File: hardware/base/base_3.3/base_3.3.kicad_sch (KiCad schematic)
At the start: 8 parts, among them IC1 single_pad_smd, IC2 single_pad_smd, J1 Conn 1, J2 Conn 2

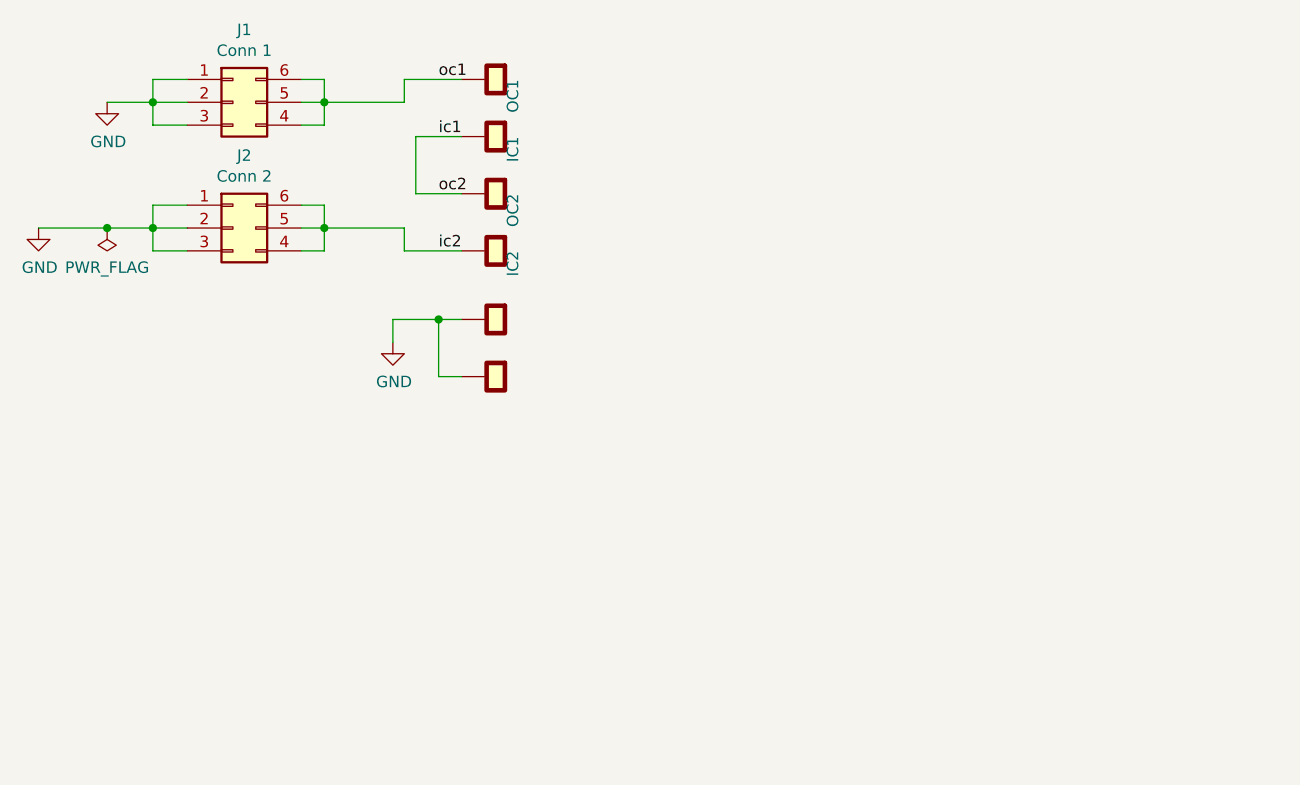
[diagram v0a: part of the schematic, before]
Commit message: Base 3.3 updated to v2
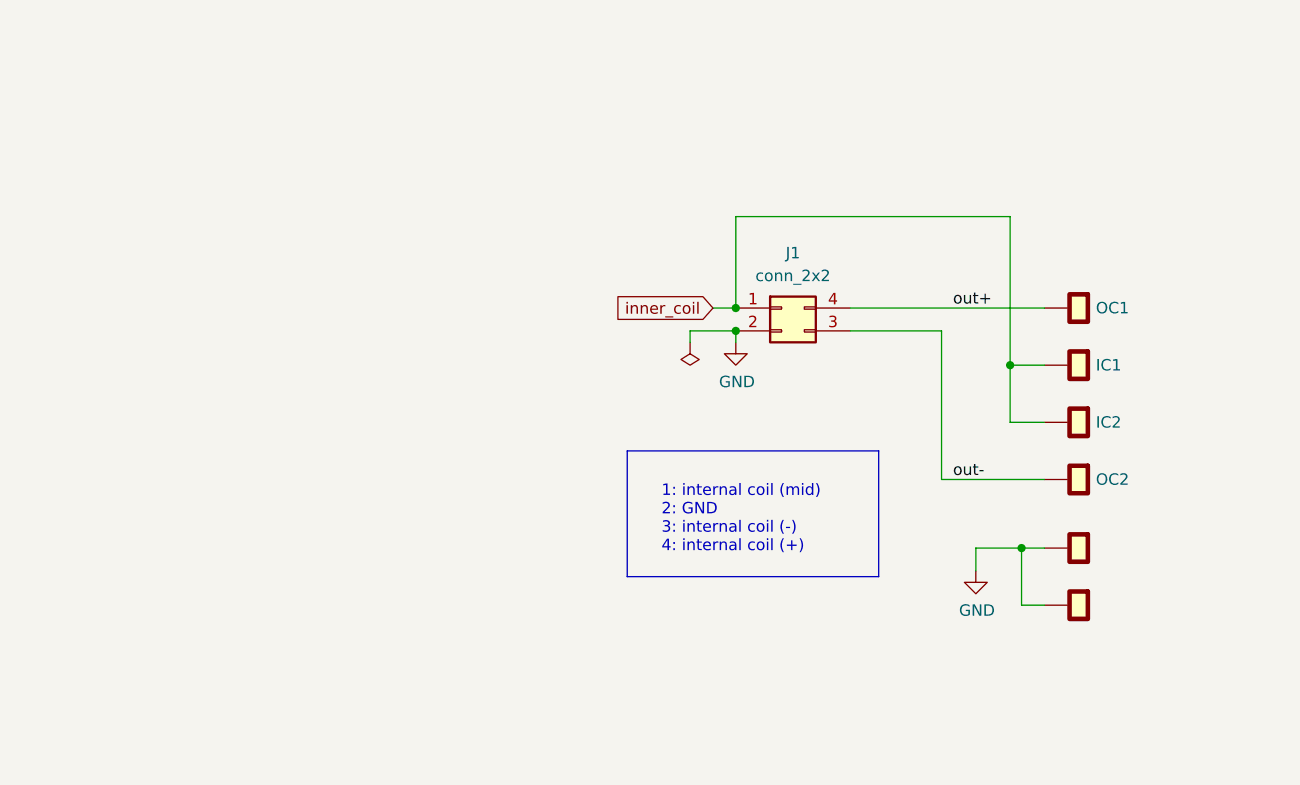
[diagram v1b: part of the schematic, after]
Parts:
- removed J1: Conn 1, cycfi_library:pin_header_2x3p_1.00mm_smd_vertical, symbol Connector_Generic:Conn_02x03_Counter_Clockwise
- removed J2: Conn 2, cycfi_library:pin_header_2x3p_1.00mm_smd_vertical, symbol Connector_Generic:Conn_02x03_Counter_Clockwise
- added J1: conn_2x2, cycfi_library:pin_header_2x2p_2.00mm_smd_vertical, symbol Connector_Generic:Conn_02x02_Counter_Clockwise
- H5, H6: value single_pad_smd -> single_pad; footprint cycfi_library:single-pad-3x2 -> xr_spectra_library:rail_slot_3.3; symbol cycfi_library:single_pad_smd -> cycfi_library:single_pad
- IC1, IC2, OC1, OC2: value single_pad_smd -> single_pad; footprint cycfi_library:single-pad-2x2-th -> cycfi_library:single-pad-1.6x1.6_circular; symbol cycfi_library:single_pad_smd -> cycfi_library:single_pad
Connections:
- net ic2 is gone; now on net inner_coil: IC2.1
- net GND: now also J1.2 (Pin_2)
- net ic1 renamed inner_coil
- net inner_coil: now also J1.1 (Pin_1); no longer OC2.1
- net oc1 renamed out+
- net out+: now also J1.4 (Pin_4)
- new net out-: J1.3 (Pin_3), OC2.1
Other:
- note added: "1: internal coil (mid) 2: GND 3: internal coil (-) 4: internal coil (+)"
- moved on the sheet: IC1, IC2, OC1, OC2

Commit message: fixed schematics
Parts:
- renumbered OC1 to IC1, OC2 to IC2, IC1 to OC1, IC2 to OC2
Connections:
- net inner_coil renamed middle_coil
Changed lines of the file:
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@@
     (stroke (width 0) (type default) (color 0 0 0 0))
   )
-  (polyline (pts (xy 123.825 86.995) (xy 123.825 100.965))
+  (polyline (pts (xy 123.19 87.63) (xy 123.19 101.6))
     (stroke (width 0) (type default) (color 0 0 0 0))
   )
@@
     (stroke (width 0) (type default) (color 0 0 0 0))
   )
-  (polyline (pts (xy 123.825 86.995) (xy 151.765 86.995))
+  (polyline (pts (xy 123.19 87.63) (xy 152.4 87.63))
     (stroke (width 0) (type default) (color 0 0 0 0))
   )
@@
     (stroke (width 0) (type default) (color 0 0 0 0))
   )
-  (polyline (pts (xy 151.765 100.965) (xy 123.825 100.965))
+  (polyline (pts (xy 152.4 101.6) (xy 123.19 101.6))
     (stroke (width 0) (type default) (color 0 0 0 0))
   )
@@
     (stroke (width 0) (type default) (color 0 0 0 0))
   )
-  (polyline (pts (xy 151.765 86.995) (xy 151.765 100.965))
+  (polyline (pts (xy 152.4 87.63) (xy 152.4 101.6))
     (stroke (width 0) (type default) (color 0 0 0 0))
   )
@@
     (effects (font (size 1.27 1.27)) (justify left bottom))
   )
-  (global_label "inner_coil" (shape input) (at 133.35 71.12 180) (fields_autoplaced)
+  (global_label "middle_coil" (shape input) (at 133.35 71.12 180) (fields_autoplaced)
     (effects (font (size 1.27 1.27)) (justify right))
-    (property "Intersheet References" "${INTERSHEET_REFS}" (id 0) (at 121.7729 71.0406 0)
+    (property "Intersheet References" "${INTERSHEET_REFS}" (id 0) (at 120.2006 71.0406 0)
       (effects (font (size 1.27 1.27)) (justify right) hide)
     )
@@
   (symbol (lib_id "cycfi_library:single_pad") (at 172.72 71.12 270) (unit 1)
     (in_bom yes) (on_board yes)
-    (property "Reference" "OC1" (id 0) (at 175.895 71.12 90)
+    (property "Reference" "IC1" (id 0) (at 175.895 71.12 90)
       (effects (font (size 1.27 1.27)) (justify left))
     )
@@
   (symbol (lib_id "cycfi_library:single_pad") (at 172.72 77.47 270) (unit 1)
     (in_bom yes) (on_board yes)
-    (property "Reference" "IC1" (id 0) (at 175.895 77.47 90)
+    (property "Reference" "OC1" (id 0) (at 175.895 77.47 90)
       (effects (font (size 1.27 1.27)) (justify left))
     )
@@
   (symbol (lib_id "cycfi_library:single_pad") (at 172.72 90.17 270) (unit 1)
     (in_bom yes) (on_board yes)
-    (property "Reference" "OC2" (id 0) (at 175.895 90.17 90)
+    (property "Reference" "IC2" (id 0) (at 175.895 90.17 90)
       (effects (font (size 1.27 1.27)) (justify left))
     )
@@
   (symbol (lib_id "cycfi_library:single_pad") (at 172.72 83.82 270) (unit 1)
     (in_bom yes) (on_board yes)
-    (property "Reference" "IC2" (id 0) (at 175.895 83.82 90)
+    (property "Reference" "OC2" (id 0) (at 175.895 83.82 90)
       (effects (font (size 1.27 1.27)) (justify left))
     )
@@
       (reference "H6") (unit 1) (value "single_pad") (footprint "xr_spectra_library:rail_slot_3.3")
     )
-    (path "/00000000-0000-0000-0000-000061122fed"
+    (path "/00000000-0000-0000-0000-000061122909"
       (reference "IC1") (unit 1) (value "single_pad") (footprint "cycfi_library:single-pad-1.6x1.6_circular")
     )
-    (path "/00000000-0000-0000-0000-0000611302a2"
+    (path "/00000000-0000-0000-0000-00006112ffae"
       (reference "IC2") (unit 1) (value "single_pad") (footprint "cycfi_library:single-pad-1.6x1.6_circular")
     )
@@
       (reference "J1") (unit 1) (value "conn_2x2") (footprint "cycfi_library:pin_header_2x2p_2.00mm_smd_vertical")
     )
-    (path "/00000000-0000-0000-0000-000061122909"
+    (path "/00000000-0000-0000-0000-000061122fed"
       (reference "OC1") (unit 1) (value "single_pad") (footprint "cycfi_library:single-pad-1.6x1.6_circular")
     )
-    (path "/00000000-0000-0000-0000-00006112ffae"
+    (path "/00000000-0000-0000-0000-0000611302a2"
       (reference "OC2") (unit 1) (value "single_pad") (footprint "cycfi_library:single-pad-1.6x1.6_circular")
     )

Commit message: Base 3.3 v3
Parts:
- removed H5, H6: single_pad, xr_spectra_library:rail_slot_3.3, symbol cycfi_library:single_pad
- IC1, IC2, OC1, OC2: footprint cycfi_library:single-pad-1.6x1.6_circular -> Connector_PinHeader_2.54mm:PinHeader_1x01_P2.54mm_Vertical
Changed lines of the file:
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@@
 (kicad_sch (version 20211123) (generator eeschema)
   (paper "A4")
-  (junction (at 167.64 97.79) (diameter 0) (color 0 0 0 0)
-  )
   (junction (at 166.37 77.47) (diameter 0) (color 0 0 0 0)
   )
@@
     (stroke (width 0) (type default) (color 0 0 0 0))
   )
-  (wire (pts (xy 170.18 97.79) (xy 167.64 97.79))
-    (stroke (width 0) (type default) (color 0 0 0 0))
-  )
   (wire (pts (xy 130.81 73.66) (xy 135.89 73.66))
     (stroke (width 0) (type default) (color 0 0 0 0))
@@
     (stroke (width 0) (type default) (color 0 0 0 0))
   )
-  (wire (pts (xy 167.64 104.14) (xy 167.64 97.79))
-    (stroke (width 0) (type default) (color 0 0 0 0))
-  )
   (wire (pts (xy 148.59 73.66) (xy 158.75 73.66))
     (stroke (width 0) (type default) (color 0 0 0 0))
@@
     (stroke (width 0) (type default) (color 0 0 0 0))
   )
-  (wire (pts (xy 162.56 97.79) (xy 162.56 100.33))
-    (stroke (width 0) (type default) (color 0 0 0 0))
-  )
-  (wire (pts (xy 170.18 104.14) (xy 167.64 104.14))
-    (stroke (width 0) (type default) (color 0 0 0 0))
-  )
   (polyline (pts (xy 152.4 101.6) (xy 123.19 101.6))
-    (stroke (width 0) (type default) (color 0 0 0 0))
-  )
-  (wire (pts (xy 167.64 97.79) (xy 162.56 97.79))
     (stroke (width 0) (type default) (color 0 0 0 0))
   )
@@
       (effects (font (size 1.27 1.27)) hide)
     )
-    (property "Footprint" "cycfi_library:single-pad-1.6x1.6_circular" (id 2) (at 172.72 71.12 0)
+    (property "Footprint" "Connector_PinHeader_2.54mm:PinHeader_1x01_P2.54mm_Vertical" (id 2) (at 172.72 71.12 0)
       (effects (font (size 1.27 1.27)) hide)
     )
@@
       (effects (font (size 1.27 1.27)) hide)
     )
-    (property "Footprint" "cycfi_library:single-pad-1.6x1.6_circular" (id 2) (at 172.72 77.47 0)
+    (property "Footprint" "Connector_PinHeader_2.54mm:PinHeader_1x01_P2.54mm_Vertical" (id 2) (at 172.72 77.47 0)
       (effects (font (size 1.27 1.27)) hide)
     )
@@
     )
     (property "Datasheet" "~" (id 3) (at 130.81 74.93 0)
-      (effects (font (size 1.27 1.27)) hide)
-    )
-    (pin "1")
-  )
-  (symbol (lib_id "cycfi_library:single_pad") (at 172.72 97.79 270) (unit 1)
-    (in_bom yes) (on_board yes)
-    (property "Reference" "H5" (id 0) (at 175.895 97.79 0)
-      (effects (font (size 1.27 1.27)) (justify left) hide)
-    )
-    (property "Value" "single_pad" (id 1) (at 177.8 97.79 0)
-      (effects (font (size 1.27 1.27)) hide)
-    )
-    (property "Footprint" "xr_spectra_library:rail_slot_3.3" (id 2) (at 172.72 97.79 0)
-      (effects (font (size 1.27 1.27)) hide)
-    )
-    (property "Datasheet" "~" (id 3) (at 172.72 97.79 0)
-      (effects (font (size 1.27 1.27)) hide)
-    )
-    (pin "1")
-  )
-  (symbol (lib_id "power:GND") (at 162.56 100.33 0) (unit 1)
-    (in_bom yes) (on_board yes)
-    (property "Reference" "#PWR03" (id 0) (at 162.56 106.68 0)
-      (effects (font (size 1.27 1.27)) hide)
-    )
-    (property "Value" "GND" (id 1) (at 162.687 104.7242 0))
-    (property "Footprint" "" (id 2) (at 162.56 100.33 0)
-      (effects (font (size 1.27 1.27)) hide)
-    )
-    (property "Datasheet" "" (id 3) (at 162.56 100.33 0)
       (effects (font (size 1.27 1.27)) hide)
     )
@@
       (effects (font (size 1.27 1.27)) hide)
     )
-    (property "Footprint" "cycfi_library:single-pad-1.6x1.6_circular" (id 2) (at 172.72 90.17 0)
+    (property "Footprint" "Connector_PinHeader_2.54mm:PinHeader_1x01_P2.54mm_Vertical" (id 2) (at 172.72 90.17 0)
       (effects (font (size 1.27 1.27)) hide)
     )
@@
       (effects (font (size 1.27 1.27)) hide)
     )
-    (property "Footprint" "cycfi_library:single-pad-1.6x1.6_circular" (id 2) (at 172.72 83.82 0)
+    (property "Footprint" "Connector_PinHeader_2.54mm:PinHeader_1x01_P2.54mm_Vertical" (id 2) (at 172.72 83.82 0)
       (effects (font (size 1.27 1.27)) hide)
     )
     (property "Datasheet" "~" (id 3) (at 172.72 83.82 0)
-      (effects (font (size 1.27 1.27)) hide)
-    )
-    (pin "1")
-  )
-  (symbol (lib_id "cycfi_library:single_pad") (at 172.72 104.14 270) (unit 1)
-    (in_bom yes) (on_board yes)
-    (property "Reference" "H6" (id 0) (at 175.895 104.14 0)
-      (effects (font (size 1.27 1.27)) (justify left) hide)
-    )
-    (property "Value" "single_pad" (id 1) (at 177.8 104.14 0)
-      (effects (font (size 1.27 1.27)) hide)
-    )
-    (property "Footprint" "xr_spectra_library:rail_slot_3.3" (id 2) (at 172.72 104.14 0)
-      (effects (font (size 1.27 1.27)) hide)
-    )
-    (property "Datasheet" "~" (id 3) (at 172.72 104.14 0)
       (effects (font (size 1.27 1.27)) hide)
     )
@@
       (reference "#PWR01") (unit 1) (value "GND") (footprint "")
     )
-    (path "/00000000-0000-0000-0000-00006112c732"
-      (reference "#PWR03") (unit 1) (value "GND") (footprint "")
-    )
-    (path "/00000000-0000-0000-0000-00006112bc09"
-      (reference "H5") (unit 1) (value "single_pad") (footprint "xr_spectra_library:rail_slot_3.3")
-    )
-    (path "/00000000-0000-0000-0000-00006114c19e"
-      (reference "H6") (unit 1) (value "single_pad") (footprint "xr_spectra_library:rail_slot_3.3")
-    )
     (path "/00000000-0000-0000-0000-000061122909"
-      (reference "IC1") (unit 1) (value "single_pad") (footprint "cycfi_library:single-pad-1.6x1.6_circular")
+      (reference "IC1") (unit 1) (value "single_pad") (footprint "Connector_PinHeader_2.54mm:PinHeader_1x01_P2.54mm_Vertical")
     )
     (path "/00000000-0000-0000-0000-00006112ffae"
-      (reference "IC2") (unit 1) (value "single_pad") (footprint "cycfi_library:single-pad-1.6x1.6_circular")
+      (reference "IC2") (unit 1) (value "single_pad") (footprint "Connector_PinHeader_2.54mm:PinHeader_1x01_P2.54mm_Vertical")
     )
     (path "/8d2043d0-1e2a-47a8-b40c-1d3c6b8242cf"
@@
     )
     (path "/00000000-0000-0000-0000-000061122fed"
-      (reference "OC1") (unit 1) (value "single_pad") (footprint "cycfi_library:single-pad-1.6x1.6_circular")
+      (reference "OC1") (unit 1) (value "single_pad") (footprint "Connector_PinHeader_2.54mm:PinHeader_1x01_P2.54mm_Vertical")
     )
     (path "/00000000-0000-0000-0000-0000611302a2"
-      (reference "OC2") (unit 1) (value "single_pad") (footprint "cycfi_library:single-pad-1.6x1.6_circular")
-    )
-  )
+      (reference "OC2") (unit 1) (value "single_pad") (footprint "Connector_PinHeader_2.54mm:PinHeader_1x01_P2.54mm_Vertical")
+    )
+  )
